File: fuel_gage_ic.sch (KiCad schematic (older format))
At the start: 8 parts, among them IC4 BQ27426YZFR

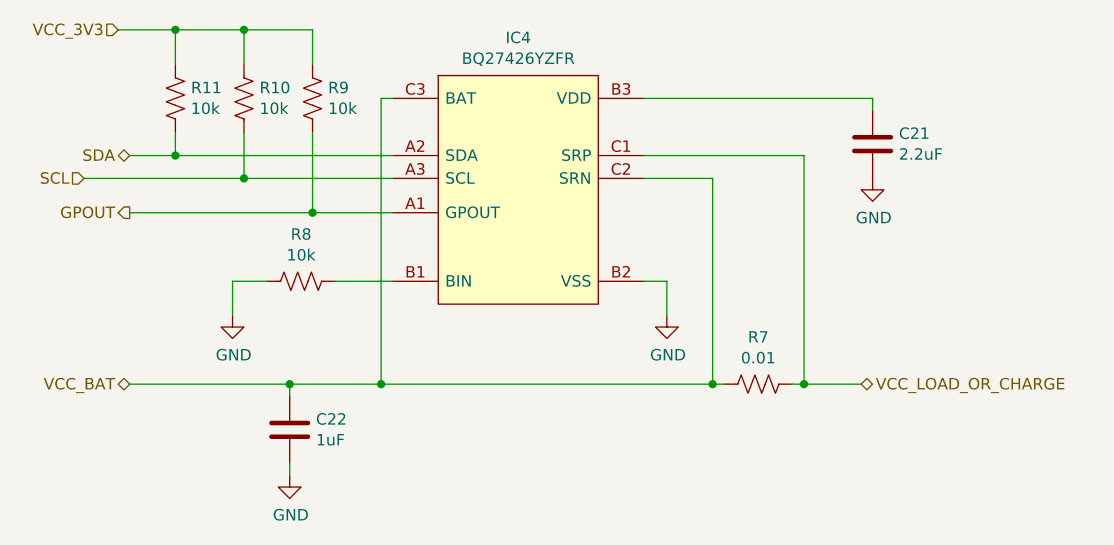
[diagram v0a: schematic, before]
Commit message: Fixed some symbols, assigned some footprints, and made wire labels
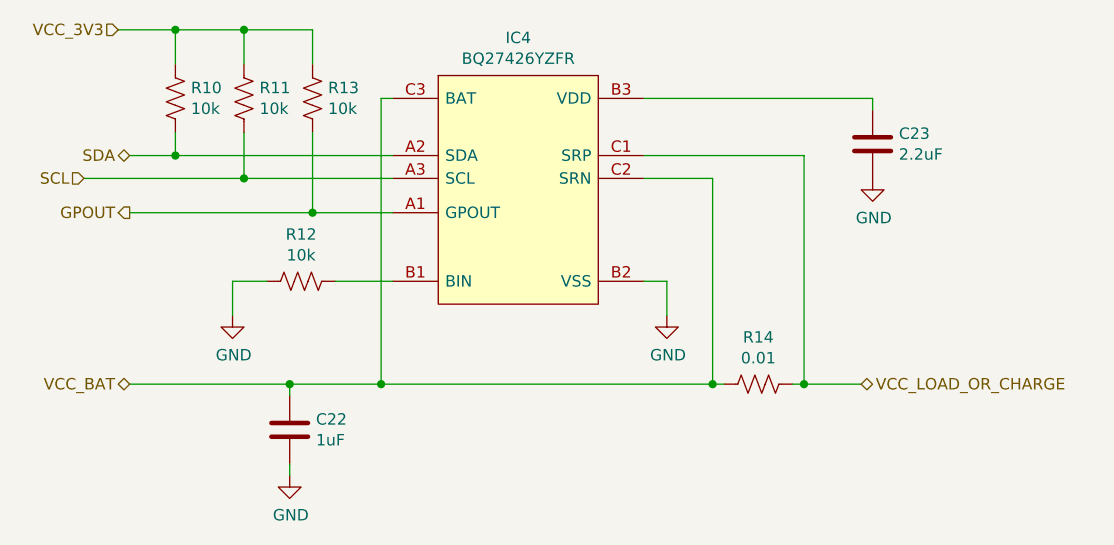
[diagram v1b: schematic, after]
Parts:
- IC4: footprint BGA9C50P3X3_158X162X62 -> FuelGage_IC:BGA9C50P3X3_158X162X62
- renumbered C21 to C23, R11 to R10, R10 to R11, R8 to R12, R9 to R13, R7 to R14
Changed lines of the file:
@@
 F 0 "IC4" H 5750 3965 50  0000 C CNN
 F 1 "BQ27426YZFR" H 5750 3874 50  0000 C CNN
-F 2 "BGA9C50P3X3_158X162X62" H 5400 2650 50  0001 L CNN
+F 2 "FuelGage_IC:BGA9C50P3X3_158X162X62" H 5400 2650 50  0001 L CNN
 F 3 "http://www.ti.com/lit/gpn/bq27426" H 5400 2550 50  0001 L CNN
 F 4 "Single cell System-Side Battery Fuel (Gas) Gauge w/Pre-programmed Chemistry Profile" H 5400 2450 50  0001 L CNN "Description"
@@
 AR Path="/60C7453A" Ref="#PWR?"  Part="1"
 AR Path="/60BA4931/60C7453A" Ref="#PWR?"  Part="1"
-AR Path="/60BA4931/60C6FA96/60C7453A" Ref="#PWR?"  Part="1"
-F 0 "#PWR?" H 6400 4000 50  0001 C CNN
+AR Path="/60BA4931/60C6FA96/60C7453A" Ref="#PWR028"  Part="1"
+F 0 "#PWR028" H 6400 4000 50  0001 C CNN
 F 1 "GND" H 6405 4077 50  0000 C CNN
 F 2 "" H 6400 4250 50  0001 C CNN
@@
 AR Path="/60C74548" Ref="R?"  Part="1"
 AR Path="/60BA4931/60C74548" Ref="R?"  Part="1"
-AR Path="/60BA4931/60C6FA96/60C74548" Ref="R7"  Part="1"
-F 0 "R7" V 6595 4550 50  0000 C CNN
+AR Path="/60BA4931/60C6FA96/60C74548" Ref="R14"  Part="1"
+F 0 "R14" V 6595 4550 50  0000 C CNN
 F 1 "0.01" V 6686 4550 50  0000 C CNN
 F 2 "" V 6840 4540 50  0001 C CNN
@@
 AR Path="/60C74551" Ref="R?"  Part="1"
 AR Path="/60BA4931/60C74551" Ref="R?"  Part="1"
-AR Path="/60BA4931/60C6FA96/60C74551" Ref="R11"  Part="1"
-F 0 "R11" H 4318 3346 50  0000 L CNN
+AR Path="/60BA4931/60C6FA96/60C74551" Ref="R10"  Part="1"
+F 0 "R10" H 4318 3346 50  0000 L CNN
 F 1 "10k" H 4318 3255 50  0000 L CNN
 F 2 "" V 4290 3290 50  0001 C CNN
@@
 AR Path="/60C74557" Ref="R?"  Part="1"
 AR Path="/60BA4931/60C74557" Ref="R?"  Part="1"
-AR Path="/60BA4931/60C6FA96/60C74557" Ref="R10"  Part="1"
-F 0 "R10" H 4618 3346 50  0000 L CNN
+AR Path="/60BA4931/60C6FA96/60C74557" Ref="R11"  Part="1"
+F 0 "R11" H 4618 3346 50  0000 L CNN
 F 1 "10k" H 4618 3255 50  0000 L CNN
 F 2 "" V 4590 3290 50  0001 C CNN
@@
 AR Path="/60C7456D" Ref="C?"  Part="1"
 AR Path="/60BA4931/60C7456D" Ref="C?"  Part="1"
-AR Path="/60BA4931/60C6FA96/60C7456D" Ref="C21"  Part="1"
-F 0 "C21" H 7415 3546 50  0000 L CNN
+AR Path="/60BA4931/60C6FA96/60C7456D" Ref="C23"  Part="1"
+F 0 "C23" H 7415 3546 50  0000 L CNN
 F 1 "2.2uF" H 7415 3455 50  0000 L CNN
 F 2 "" H 7338 3350 50  0001 C CNN
@@
 AR Path="/60C74573" Ref="#PWR?"  Part="1"
 AR Path="/60BA4931/60C74573" Ref="#PWR?"  Part="1"
-AR Path="/60BA4931/60C6FA96/60C74573" Ref="#PWR?"  Part="1"
-F 0 "#PWR?" H 7300 3400 50  0001 C CNN
+AR Path="/60BA4931/60C6FA96/60C74573" Ref="#PWR029"  Part="1"
+F 0 "#PWR029" H 7300 3400 50  0001 C CNN
 F 1 "GND" H 7305 3477 50  0000 C CNN
 F 2 "" H 7300 3650 50  0001 C CNN
@@
 AR Path="/60C7457B" Ref="#PWR?"  Part="1"
 AR Path="/60BA4931/60C7457B" Ref="#PWR?"  Part="1"
-AR Path="/60BA4931/60C6FA96/60C7457B" Ref="#PWR?"  Part="1"
-F 0 "#PWR?" H 4500 4000 50  0001 C CNN
+AR Path="/60BA4931/60C6FA96/60C7457B" Ref="#PWR026"  Part="1"
+F 0 "#PWR026" H 4500 4000 50  0001 C CNN
 F 1 "GND" H 4505 4077 50  0000 C CNN
 F 2 "" H 4500 4250 50  0001 C CNN
@@
 AR Path="/60C74581" Ref="R?"  Part="1"
 AR Path="/60BA4931/60C74581" Ref="R?"  Part="1"
-AR Path="/60BA4931/60C6FA96/60C74581" Ref="R8"  Part="1"
-F 0 "R8" V 4595 4100 50  0000 C CNN
+AR Path="/60BA4931/60C6FA96/60C74581" Ref="R12"  Part="1"
+F 0 "R12" V 4595 4100 50  0000 C CNN
 F 1 "10k" V 4686 4100 50  0000 C CNN
 F 2 "" V 4840 4090 50  0001 C CNN
@@
 AR Path="/60C7458F" Ref="R?"  Part="1"
 AR Path="/60BA4931/60C7458F" Ref="R?"  Part="1"
-AR Path="/60BA4931/60C6FA96/60C7458F" Ref="R9"  Part="1"
-F 0 "R9" H 4918 3346 50  0000 L CNN
+AR Path="/60BA4931/60C6FA96/60C7458F" Ref="R13"  Part="1"
+F 0 "R13" H 4918 3346 50  0000 L CNN
 F 1 "10k" H 4918 3255 50  0000 L CNN
 F 2 "" V 4890 3290 50  0001 C CNN
@@
 SDA
 $Comp
-L power:GND #PWR?
+L power:GND #PWR027
 U 1 1 60C8E3F9
 P 4750 4950
-F 0 "#PWR?" H 4750 4700 50  0001 C CNN
+F 0 "#PWR027" H 4750 4700 50  0001 C CNN
 F 1 "GND" H 4755 4777 50  0000 C CNN
 F 2 "" H 4750 4950 50  0001 C CNN

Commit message: Chose more parts and added more footprints. Have some resistors and all the capacitors to go
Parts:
- R10, R11, R12, R13: footprint (none) -> Resistor_SMD:R_0402_1005Metric
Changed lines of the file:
@@
 F 0 "R10" H 4318 3346 50  0000 L CNN
 F 1 "10k" H 4318 3255 50  0000 L CNN
-F 2 "" V 4290 3290 50  0001 C CNN
+F 2 "Resistor_SMD:R_0402_1005Metric" V 4290 3290 50  0001 C CNN
 F 3 "~" H 4250 3300 50  0001 C CNN
 	1    4250 3300
@@
 F 0 "R11" H 4618 3346 50  0000 L CNN
 F 1 "10k" H 4618 3255 50  0000 L CNN
-F 2 "" V 4590 3290 50  0001 C CNN
+F 2 "Resistor_SMD:R_0402_1005Metric" V 4590 3290 50  0001 C CNN
 F 3 "~" H 4550 3300 50  0001 C CNN
 	1    4550 3300
@@
 F 0 "R12" V 4595 4100 50  0000 C CNN
 F 1 "10k" V 4686 4100 50  0000 C CNN
-F 2 "" V 4840 4090 50  0001 C CNN
+F 2 "Resistor_SMD:R_0402_1005Metric" V 4840 4090 50  0001 C CNN
 F 3 "~" H 4800 4100 50  0001 C CNN
 	1    4800 4100
@@
 F 0 "R13" H 4918 3346 50  0000 L CNN
 F 1 "10k" H 4918 3255 50  0000 L CNN
-F 2 "" V 4890 3290 50  0001 C CNN
+F 2 "Resistor_SMD:R_0402_1005Metric" V 4890 3290 50  0001 C CNN
 F 3 "~" H 4850 3300 50  0001 C CNN
 	1    4850 3300

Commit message: Finished assigning footprints, and generated netlist
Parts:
- C22, C23: footprint (none) -> Capacitor_SMD:C_0603_1608Metric
- R10, R11, R12, R13: footprint Resistor_SMD:R_0402_1005Metric -> Resistor_SMD:R_1206_3216Metric
- R14: footprint (none) -> Resistor_SMD:R_1206_3216Metric
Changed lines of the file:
@@
 F 0 "C22" H 4865 4796 50  0000 L CNN
 F 1 "1uF" H 4865 4705 50  0000 L CNN
-F 2 "" H 4788 4600 50  0001 C CNN
+F 2 "Capacitor_SMD:C_0603_1608Metric" H 4788 4600 50  0001 C CNN
 F 3 "~" H 4750 4750 50  0001 C CNN
 	1    4750 4750
@@
 F 0 "R14" V 6595 4550 50  0000 C CNN
 F 1 "0.01" V 6686 4550 50  0000 C CNN
-F 2 "" V 6840 4540 50  0001 C CNN
+F 2 "Resistor_SMD:R_1206_3216Metric" V 6840 4540 50  0001 C CNN
 F 3 "~" H 6800 4550 50  0001 C CNN
 	1    6800 4550
@@
 F 0 "R10" H 4318 3346 50  0000 L CNN
 F 1 "10k" H 4318 3255 50  0000 L CNN
-F 2 "Resistor_SMD:R_0402_1005Metric" V 4290 3290 50  0001 C CNN
+F 2 "Resistor_SMD:R_1206_3216Metric" V 4290 3290 50  0001 C CNN
 F 3 "~" H 4250 3300 50  0001 C CNN
 	1    4250 3300
@@
 F 0 "R11" H 4618 3346 50  0000 L CNN
 F 1 "10k" H 4618 3255 50  0000 L CNN
-F 2 "Resistor_SMD:R_0402_1005Metric" V 4590 3290 50  0001 C CNN
+F 2 "Resistor_SMD:R_1206_3216Metric" V 4590 3290 50  0001 C CNN
 F 3 "~" H 4550 3300 50  0001 C CNN
 	1    4550 3300
@@
 F 0 "C23" H 7415 3546 50  0000 L CNN
 F 1 "2.2uF" H 7415 3455 50  0000 L CNN
-F 2 "" H 7338 3350 50  0001 C CNN
+F 2 "Capacitor_SMD:C_0603_1608Metric" H 7338 3350 50  0001 C CNN
 F 3 "~" H 7300 3500 50  0001 C CNN
 	1    7300 3500
@@
 F 0 "R12" V 4595 4100 50  0000 C CNN
 F 1 "10k" V 4686 4100 50  0000 C CNN
-F 2 "Resistor_SMD:R_0402_1005Metric" V 4840 4090 50  0001 C CNN
+F 2 "Resistor_SMD:R_1206_3216Metric" V 4840 4090 50  0001 C CNN
 F 3 "~" H 4800 4100 50  0001 C CNN
 	1    4800 4100
@@
 F 0 "R13" H 4918 3346 50  0000 L CNN
 F 1 "10k" H 4918 3255 50  0000 L CNN
-F 2 "Resistor_SMD:R_0402_1005Metric" V 4890 3290 50  0001 C CNN
+F 2 "Resistor_SMD:R_1206_3216Metric" V 4890 3290 50  0001 C CNN
 F 3 "~" H 4850 3300 50  0001 C CNN
 	1    4850 3300
